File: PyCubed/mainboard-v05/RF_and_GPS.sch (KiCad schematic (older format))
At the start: 28 parts, among them J12 Amphenol_901-144, J4 874370443, J5 Amphenol_901-144, J6 Amphenol_901-144, J7 Amphenol_901-144, U13 EP2W+, U14 S1216V8, U15 RFM9xBreakout, U23 RFM98PW, U24 RFM98PW, U9 TPS54226PWPRPWP14_2P31X2P46-L

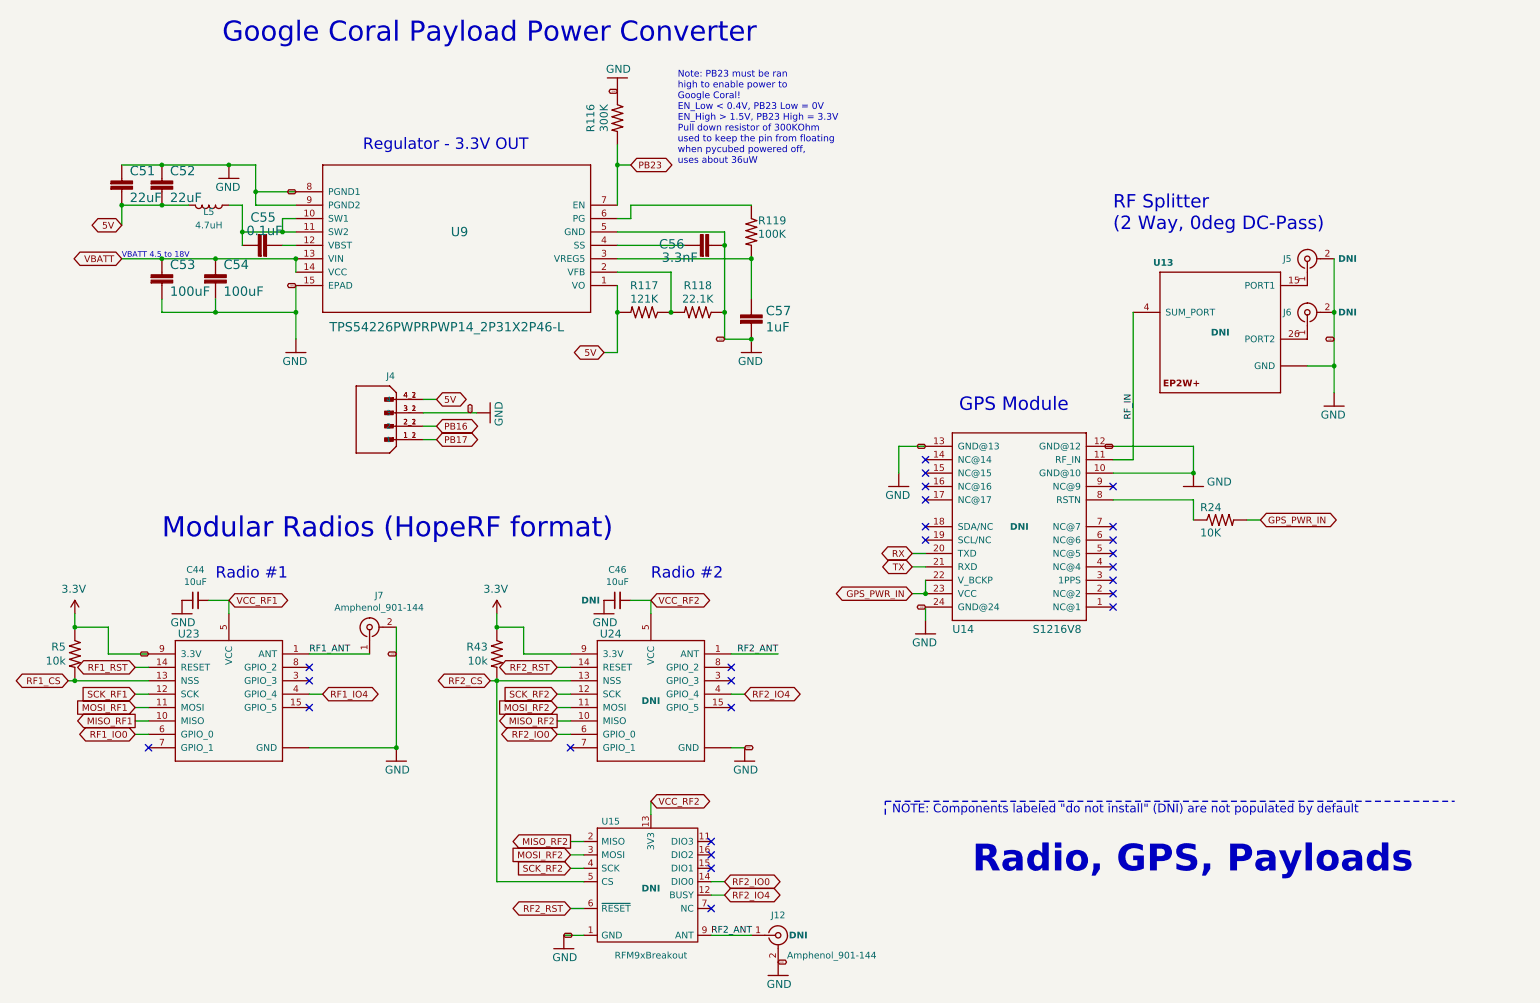
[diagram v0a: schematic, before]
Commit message: Battery board and side panels ready for CAD check and review, pycubed not finished yet
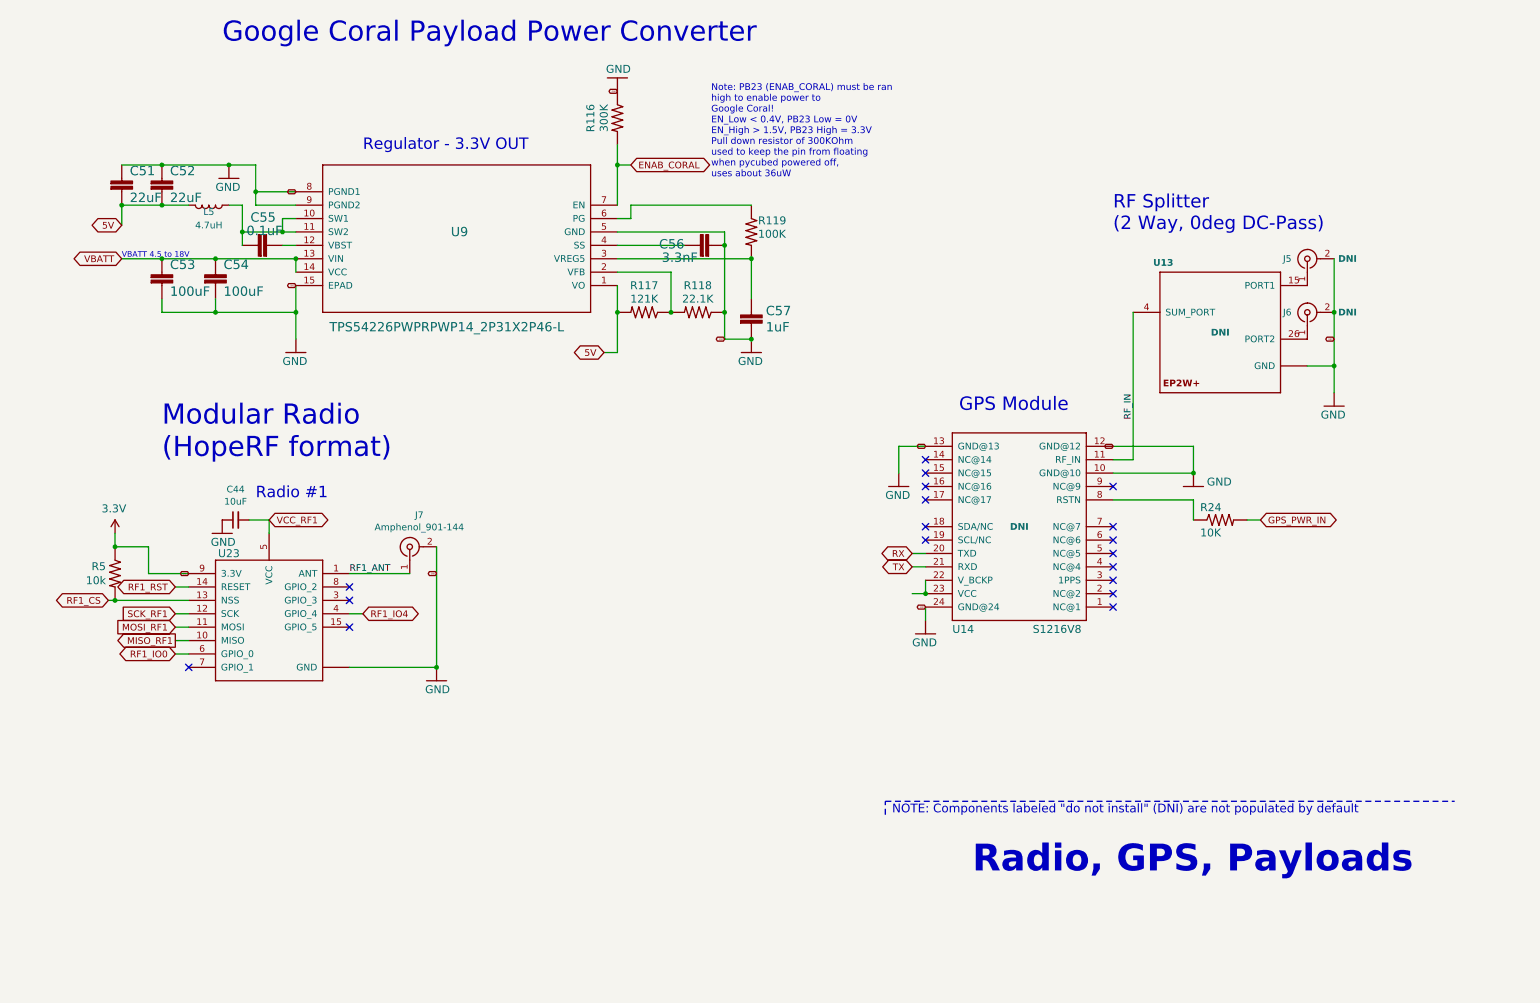
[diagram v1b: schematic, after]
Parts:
- removed C46: 10uF, Capacitor_SMD:C_0603_1608Metric, symbol Device:C_Small
- removed J12: Amphenol_901-144, Connector_Coaxial:SMA_Amphenol_901-144_Vertical, symbol Connector:Conn_Coaxial
- removed J4: 874370443, MOLEX_874370443, symbol mainboard:874370443
- removed R43: 10k, Resistor_SMD:R_0603_1608Metric, symbol mainboard:10KOHM-1_10W-1%(0603)0603
- removed U15: RFM9xBreakout, RF_Module:HOPERF_RFM9XW_SMD, symbol mainboard:RFM9xBreakout
- removed U24: RFM98PW, mainboard:RFM95PW, symbol mainboard:RFM98PW
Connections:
- net GPS_PWR_IN: no longer U14.22 (V_BCKP), U14.23 (VCC)
- net PB23 renamed ENAB_CORAL
- new net: U14.22 (V_BCKP), U14.23 (VCC)
- no-connect marks 26 -> 18
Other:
- note added: "Modular Radio \n(HopeRF format)"
- note added: "Note: PB23 (ENAB_CORAL) must be ran \nhigh to enable power to \nGoogle Coral!\nEN_Low < 0.4V, PB23 Low = 0V\nEN_High > 1.5V, PB23 High = 3.3V\nPull down resistor of 300KOhm \nused to keep the pin from floating\nwhen pycubed powered off, \nuses about 36uW"
- note removed: "Modular Radios (HopeRF format)"
- note removed: "Note: PB23 must be ran \nhigh to enable power to \nGoogle Coral!\nEN_Low < 0.4V, PB23 Low = 0V\nEN_High > 1.5V, PB23 High = 3.3V\nPull down resistor of 300KOhm \nused to keep the pin from floating\nwhen pycubed powered off, \nuses about 36uW"
- note removed: "Radio #2"
- moved on the sheet: C44, J7, R5, U23
